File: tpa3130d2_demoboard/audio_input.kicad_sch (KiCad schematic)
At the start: 5 parts, among them J1 Screw_Terminal_01x02, J3 Screw_Terminal_01x02, J5 AudioJack3_Ground_SwitchTR

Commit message: Scheme complete
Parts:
- added C100, C101, C102, C103: 1uF, symbol Device:C_Polarized
- renumbered J1 to J100, J5 to J101, J3 to J102, R1 to R100, R2 to R101
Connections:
- net GND: now also C101.2, C103.2
- net LINN: now also C103.1
- net LINP: now also C102.1
- net RINN: now also C101.1
- net RINP: now also C100.1
- net LINE_IN_CONN_L renamed IN_L
- net IN_L: now also C102.2
- net LINE_IN_CONN_R renamed IN_R
- net IN_R: now also C100.2

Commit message: Fill BOM
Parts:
- C100, C101, C102, C103: footprint (none) -> Capacitor_Tantalum_SMD:CP_EIA-3216-18_Kemet-A; Manufacturer (none) -> Kyocera AVX; Part Number (none) -> TAJA105K035RNJ
- J100, J102: Manufacturer (none) -> Ningbo Kangnex Elec; Part Number (none) -> WJ500V-5.08-2P
- R100, R101: footprint (none) -> Resistor_SMD:R_0603_1608Metric; Manufacturer (none) -> UNI-ROYAL(Uniroyal Elec); Part Number (none) -> 0603WAJ0473T5E
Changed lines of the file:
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@@
 			)
 		)
-		(property "Footprint" ""
+		(property "Footprint" "Capacitor_Tantalum_SMD:CP_EIA-3216-18_Kemet-A"
 			(at 113.03 54.3052 0)
 			(effects
@@
 			)
 		)
+		(property "Manufacturer" "Kyocera AVX"
+			(at 116.84 53.34 0)
+			(effects
+				(font
+					(size 1.27 1.27)
+				)
+				(hide yes)
+			)
+		)
+		(property "Part Number" "TAJA105K035RNJ"
+			(at 116.84 53.34 0)
+			(effects
+				(font
+					(size 1.27 1.27)
+				)
+				(hide yes)
+			)
+		)
 		(pin "1"
 		)
@@
 			)
 		)
-		(property "Footprint" ""
+		(property "Footprint" "Resistor_SMD:R_0603_1608Metric"
 			(at 73.152 60.96 90)
 			(effects
@@
 			)
 		)
+		(property "Manufacturer" "UNI-ROYAL(Uniroyal Elec)"
+			(at 74.93 60.96 0)
+			(effects
+				(font
+					(size 1.27 1.27)
+				)
+				(hide yes)
+			)
+		)
+		(property "Part Number" "0603WAJ0473T5E"
+			(at 74.93 60.96 0)
+			(effects
+				(font
+					(size 1.27 1.27)
+				)
+				(hide yes)
+			)
+		)
 		(pin "2"
 		)
@@
 			)
 		)
-		(property "Footprint" ""
+		(property "Footprint" "Capacitor_Tantalum_SMD:CP_EIA-3216-18_Kemet-A"
 			(at 113.03 67.0052 0)
 			(effects
@@
 			)
 		)
+		(property "Manufacturer" "Kyocera AVX"
+			(at 116.84 66.04 0)
+			(effects
+				(font
+					(size 1.27 1.27)
+				)
+				(hide yes)
+			)
+		)
+		(property "Part Number" "TAJA105K035RNJ"
+			(at 116.84 66.04 0)
+			(effects
+				(font
+					(size 1.27 1.27)
+				)
+				(hide yes)
+			)
+		)
 		(pin "1"
 		)
@@
 			)
 		)
-		(property "Footprint" ""
+		(property "Footprint" "Resistor_SMD:R_0603_1608Metric"
 			(at 73.152 124.46 90)
 			(effects
@@
 			)
 		)
+		(property "Manufacturer" "UNI-ROYAL(Uniroyal Elec)"
+			(at 74.93 124.46 0)
+			(effects
+				(font
+					(size 1.27 1.27)
+				)
+				(hide yes)
+			)
+		)
+		(property "Part Number" "0603WAJ0473T5E"
+			(at 74.93 124.46 0)
+			(effects
+				(font
+					(size 1.27 1.27)
+				)
+				(hide yes)
+			)
+		)
 		(pin "2"
 		)
@@
 			)
 		)
-		(property "Footprint" ""
+		(property "Footprint" "Capacitor_Tantalum_SMD:CP_EIA-3216-18_Kemet-A"
 			(at 113.03 102.5652 0)
 			(effects
@@
 			)
 		)
+		(property "Manufacturer" "Kyocera AVX"
+			(at 116.84 101.6 0)
+			(effects
+				(font
+					(size 1.27 1.27)
+				)
+				(hide yes)
+			)
+		)
+		(property "Part Number" "TAJA105K035RNJ"
+			(at 116.84 101.6 0)
+			(effects
+				(font
+					(size 1.27 1.27)
+				)
+				(hide yes)
+			)
+		)
 		(pin "1"
 		)
@@
 			)
 		)
+		(property "Manufacturer" ""
+			(at 69.85 83.82 0)
+			(effects
+				(font
+					(size 1.27 1.27)
+				)
+				(hide yes)
+			)
+		)
+		(property "Part Number" ""
+			(at 69.85 83.82 0)
+			(effects
+				(font
+					(size 1.27 1.27)
+				)
+				(hide yes)
+			)
+		)
 		(pin "RN"
 		)
@@
 			)
 		)
+		(property "Manufacturer" "Ningbo Kangnex Elec"
+			(at 59.69 55.88 0)
+			(effects
+				(font
+					(size 1.27 1.27)
+				)
+				(hide yes)
+			)
+		)
+		(property "Part Number" "WJ500V-5.08-2P"
+			(at 59.69 55.88 0)
+			(effects
+				(font
+					(size 1.27 1.27)
+				)
+				(hide yes)
+			)
+		)
 		(pin "1"
 		)
@@
 			)
 		)
+		(property "Manufacturer" "Ningbo Kangnex Elec"
+			(at 59.69 119.38 0)
+			(effects
+				(font
+					(size 1.27 1.27)
+				)
+				(hide yes)
+			)
+		)
+		(property "Part Number" "WJ500V-5.08-2P"
+			(at 59.69 119.38 0)
+			(effects
+				(font
+					(size 1.27 1.27)
+				)
+				(hide yes)
+			)
+		)
 		(pin "1"
 		)
@@
 			)
 		)
-		(property "Footprint" ""
+		(property "Footprint" "Capacitor_Tantalum_SMD:CP_EIA-3216-18_Kemet-A"
 			(at 113.03 89.8652 0)
 			(effects
@@
 			(at 116.84 88.9 0)
 			(effects
+				(font
+					(size 1.27 1.27)
+				)
+				(hide yes)
+			)
+		)
+		(property "Manufacturer" "Kyocera AVX"
+			(at 116.84 88.9 0)
+			(effects
+				(font
+					(size 1.27 1.27)
+				)
+				(hide yes)
+			)
+		)
+		(property "Part Number" "TAJA105K035RNJ"
+			(at 116.84 88.9 0)
+			(effects

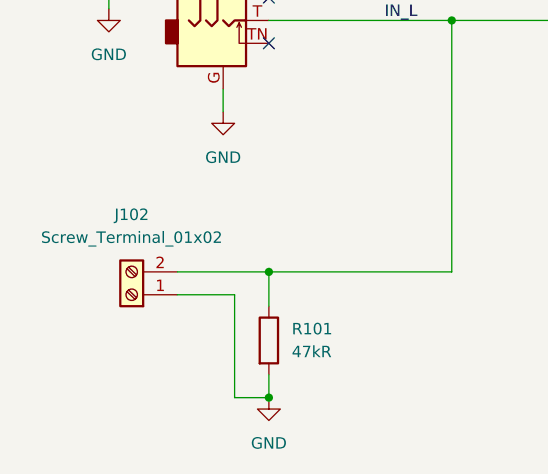
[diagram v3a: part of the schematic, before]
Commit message: Minor changes in terminal block footprint
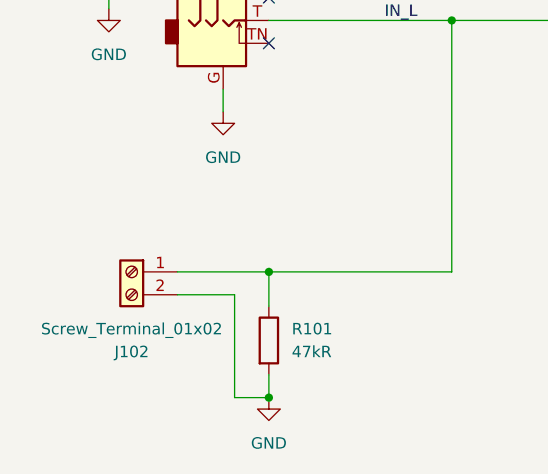
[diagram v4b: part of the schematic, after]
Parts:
- J100, J102: footprint TerminalBlock:TerminalBlock_bornier-2_P5.08mm -> tpa3130d2_demoboard:terminal_block
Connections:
- net GND: now also J102.2 (Pin_2); no longer J102.1 (Pin_1)
- net IN_L: now also J102.1 (Pin_1); no longer J102.2 (Pin_2)
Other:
- moved on the sheet: J102
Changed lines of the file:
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@@
+	)
+	(junction
+		(at 95.25 88.9)
+		(diameter 0)
+		(color 0 0 0 0)
 	)
 	(junction
@@
 	)
 	(junction
-		(at 95.25 88.9)
-		(diameter 0)
-		(color 0 0 0 0)
-	)
-	(junction
 		(at 74.93 53.34)
 		(diameter 0)
@@
 	(wire
 		(pts
-			(xy 71.12 119.38) (xy 64.77 119.38)
-		)
-		(stroke
-			(width 0)
-			(type default)
-		)
-	)
-	(wire
-		(pts
 			(xy 74.93 88.9) (xy 95.25 88.9)
 		)
@@
 	(wire
 		(pts
-			(xy 74.93 116.84) (xy 64.77 116.84)
-		)
-		(stroke
-			(width 0)
-			(type default)
-		)
-	)
-	(wire
-		(pts
 			(xy 57.15 78.74) (xy 57.15 87.63)
 		)
@@
 	(wire
 		(pts
+			(xy 64.77 116.84) (xy 74.93 116.84)
+		)
+		(stroke
+			(width 0)
+			(type default)
+		)
+	)
+	(wire
+		(pts
 			(xy 74.93 53.34) (xy 74.93 57.15)
 		)
@@
 		(pts
 			(xy 111.76 101.6) (xy 111.76 107.95)
+		)
+		(stroke
+			(width 0)
+			(type default)
+		)
+	)
+	(wire
+		(pts
+			(xy 64.77 119.38) (xy 71.12 119.38)
 		)
 		(stroke
@@
 			)
 		)
-		(property "Footprint" "TerminalBlock:TerminalBlock_bornier-2_P5.08mm"
+		(property "Footprint" "tpa3130d2_demoboard:terminal_block"
 			(at 59.69 55.88 0)
 			(effects
@@
 	(symbol
 		(lib_id "Connector:Screw_Terminal_01x02")
-		(at 59.69 119.38 180)
+		(at 59.69 116.84 0)
+		(mirror y)
 		(unit 1)
 		(exclude_from_sim no)
@@
 		(on_board yes)
 		(dnp no)
-		(fields_autoplaced yes)
 		(property "Reference" "J102"
-			(at 59.69 110.49 0)
+			(at 59.69 125.73 0)
 			(effects
 				(font
@@
 		)
 		(property "Value" "Screw_Terminal_01x02"
-			(at 59.69 113.03 0)
-			(effects
-				(font
-					(size 1.27 1.27)
-				)
-			)
-		)
-		(property "Footprint" "TerminalBlock:TerminalBlock_bornier-2_P5.08mm"
-			(at 59.69 119.38 0)
+			(at 59.69 123.19 0)
+			(effects
+				(font
+					(size 1.27 1.27)
+				)
+			)
+		)
+		(property "Footprint" "tpa3130d2_demoboard:terminal_block"
+			(at 59.69 116.84 0)
 			(effects
 				(font
@@
 		)
 		(property "Datasheet" "~"
-			(at 59.69 119.38 0)
+			(at 59.69 116.84 0)
 			(effects
 				(font
@@
 		)
 		(property "Description" "Generic screw terminal, single row, 01x02, script generated (kicad-library-utils/schlib/autogen/connector/)"
-			(at 59.69 119.38 0)
+			(at 59.69 116.84 0)
 			(effects
 				(font
@@
 		)
 		(property "Manufacturer" "Ningbo Kangnex Elec"
-			(at 59.69 119.38 0)
+			(at 59.69 116.84 0)
 			(effects
 				(font
@@
 		)
 		(property "Part Number" "WJ500V-5.08-2P"
-			(at 59.69 119.38 0)
-			(effects
-				(font
+			(at 59.69 116.84 0)
+			(effects
+				(font
